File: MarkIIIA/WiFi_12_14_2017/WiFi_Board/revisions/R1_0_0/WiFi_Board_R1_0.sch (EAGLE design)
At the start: 29 parts, among them P3 USB-B1HSB6, P4 POWER_JACKPTH, P9 44764-1201

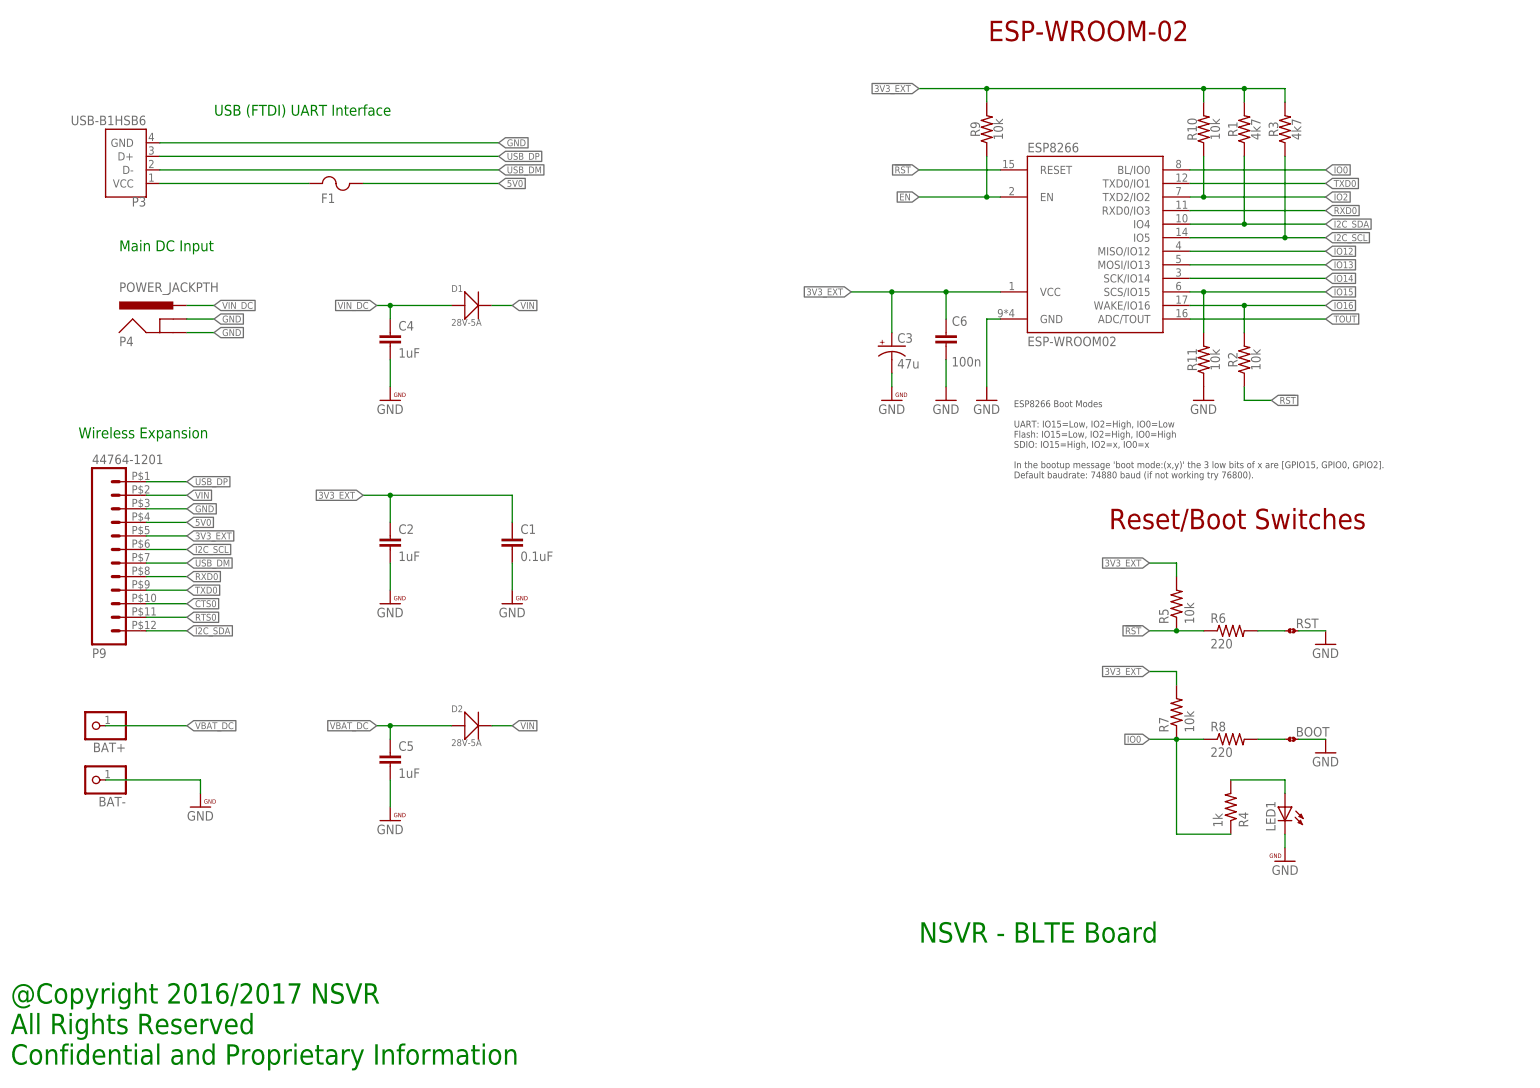
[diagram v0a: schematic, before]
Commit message: Revise WiFi Board to increase Case Clearance
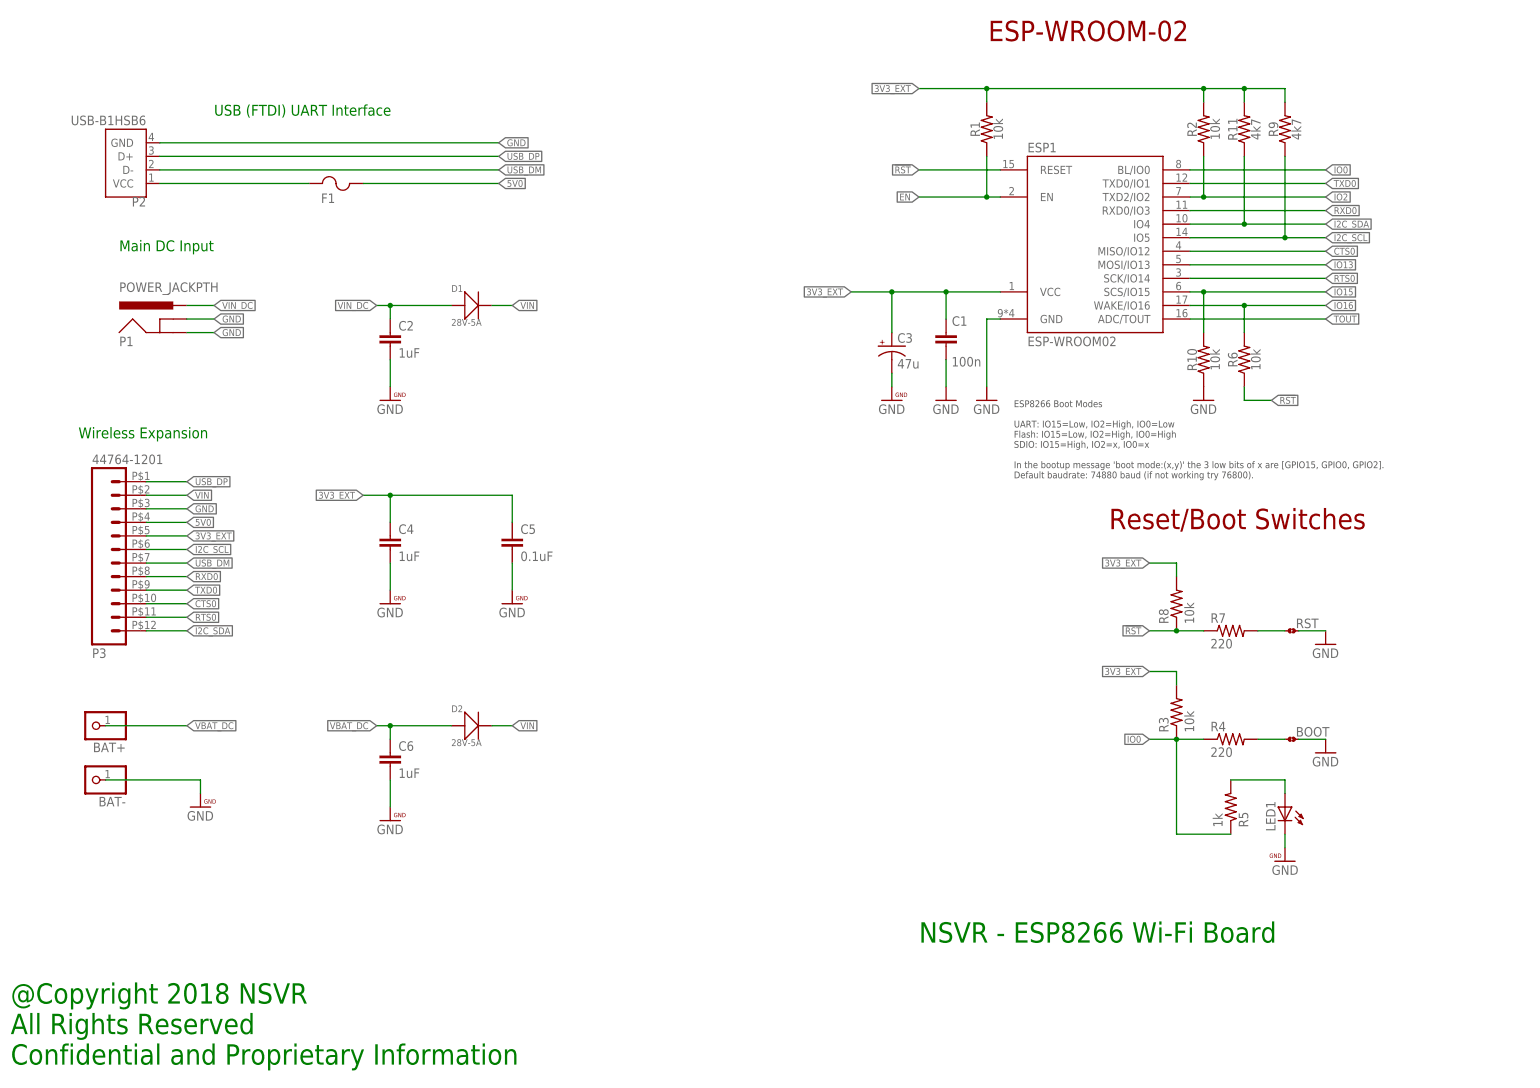
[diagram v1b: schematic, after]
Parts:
- removed P9: 44764-1201, nsvr:44764-1201
- added P2: USB-B1HSB6, USB-B1HSB6:USB-B1HSB6
- C1: value 0.1uF -> 100n
- C5: value 1uF -> 0.1uF
- C6: value 100n -> 1uF
- P3: value USB-B1HSB6 -> 44764-1201; device USB-B1HSB6:USB-B1HSB6 -> nsvr:44764-1201
- R1, R3: value 4k7 -> 10k
- R11, R9: value 10k -> 4k7
- R4: value 1k -> 220
- R5: value 10k -> 1k
- R6, R8: value 220 -> 10k
- R7: value 10k -> 220
- renumbered ESP8266 to ESP1, P4 to P1
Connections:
- removed net IO12: ESP1.MISO/IO12
- removed net IO14: ESP1.SCK/IO14
- net !RST: now also R7.1, R8.1; no longer R2.1, R5.1
- net 3V3_EXT: now also C1.2, C4.1, C5.1, P3.5, R11.2, R2.2, R8.2; no longer C1.1, C2.1, C6.2, P9.5, R10.2, R5.2, R7.2
- net 5V0: now also P3.4; no longer P9.4
- net CTS0: now also ESP1.MISO/IO12, P3.10; no longer P9.10
- net EN: now also R1.1; no longer R9.1
- net GND: now also C1.1, C6.2, P2.GND, P3.3, R10.1; no longer C1.2, C6.1, P3.GND, P9.3, R11.1
- net I2C_SCL: now also P3.6, R9.1; no longer P9.6, R3.1
- net I2C_SDA: now also P3.12, R11.1; no longer P9.12, R1.1
- net IO0: now also R3.1, R5.1; no longer R7.1, R8.1
- net IO15: now also R10.2; no longer R11.2
- net IO16: now also R6.2; no longer R2.2
- net IO2: now also R2.1; no longer R10.1
- net LED1: now also R5.2; no longer R4.2
- net N$1: now also R7.2; no longer R6.2
- net N$2: now also R4.2; no longer R8.2
- net RTS0: now also ESP1.SCK/IO14, P3.11; no longer P9.11
- net RXD0: now also P3.8; no longer P9.8
- net TXD0: now also P3.9; no longer P9.9
- net USB_DM: now also P2.D-, P3.7; no longer P3.D-, P9.7
- net USB_DP: now also P2.D+, P3.1; no longer P3.D+, P9.1
- net VBAT_DC: now also C6.1; no longer C5.1
- net VBUS_IN: now also P2.VCC; no longer P3.VCC
- net VIN: now also P3.2; no longer P9.2
- net VIN_DC: now also C2.1; no longer C4.1
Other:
- note added: "@Copyright 2018 NSVR All Rights Reserved Confidential and Proprietary Information"
- note added: "NSVR - ESP8266 Wi-Fi Board"
- note removed: "@Copyright 2016/2017 NSVR All Rights Reserved Confidential and Proprietary Information"
- note removed: "NSVR - BLTE Board"
- moved on the sheet: C1, C2, C4, C5, C6, R1, R10, R11, R2, R3, R4, R5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
